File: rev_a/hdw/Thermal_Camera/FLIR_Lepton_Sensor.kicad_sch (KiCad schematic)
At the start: 0 parts

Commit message: added lepton sensor, made some other schematic progress
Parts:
- added C1501 (x3): 0.1uF, Capacitors_SMD:C_0603, symbol Custom_Library:C_Custom
- added N?: Lepton3.5 Sensor, symbol Mechanical:Housing
- added U?: FLIR_Lepton3p5_Socket, Custom Footprints Library:MOLEX_105028-1001, symbol Custom Library:FLIR_Lepton3p5_Socket
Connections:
- new net +1.2V: C1501.1, U?.7 (VDDC)
- new net +2.8V: C1501.1, U?.19 (VDD)
- new net +3.0V: C1501.1, U?.16 (VDDIO)
- new net FLIR_CLK: U?.26 (MASTER_CLK)
- new net GND: C1501.2, C1501.2, C1501.2, U?.1 (G1), U?.10 (G10), U?.15 (G15), U?.18 (G18), U?.25 (G25), U?.27 (G27), U?.30 (G30), U?.6 (G6), U?.8 (G8), U?.9 (G9), U?.P1 (SHEILD), U?.P10 (G42), U?.P11 (G43), U?.P12 (G44), U?.P13 (G45), U?.P14 (G46), U?.P15 (G47), U?.P16 (G48), U?.P17 (G49), U?.P18 (G50), U?.P19 (G51), U?.P2 (G34), U?.P20 (G52), U?.P21 (G53), U?.P22 (G54), U?.P23 (G55), U?.P24 (G56), U?.P25 (G57), U?.P26 (G58), U?.P27 (G59), U?.P28 (G60), U?.P29 (G61), U?.P3 (G35), U?.P30 (G62), U?.P31 (G63), U?.P32 (G64), U?.P33 (G65), U?.P34 (G66), U?.P35 (G67), U?.P36 (G68), U?.P4 (G36), U?.P5 (G37), U?.P6 (G38), U?.P7 (G39), U?.P8 (G40), U?.P9 (G41)
- no-connect marks 0 -> 7
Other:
- note added: "CAUTION: +3.0V I/O"
- note added: "Power Supply Considerations: VDDC: 1.20V (1.14V min, 1.26V max), 50mVpp max ripple, 110mA max draw VDD: 2.80V (2.72V min, 2.88V max), 30mVpp max ripple, 16mA max draw VDDIO: 2.8V min, 3.1V max, 50mVpp max ripple, 310mA max draw"
- note added: "See FLIR document #110-0144-04 for I2C register map"

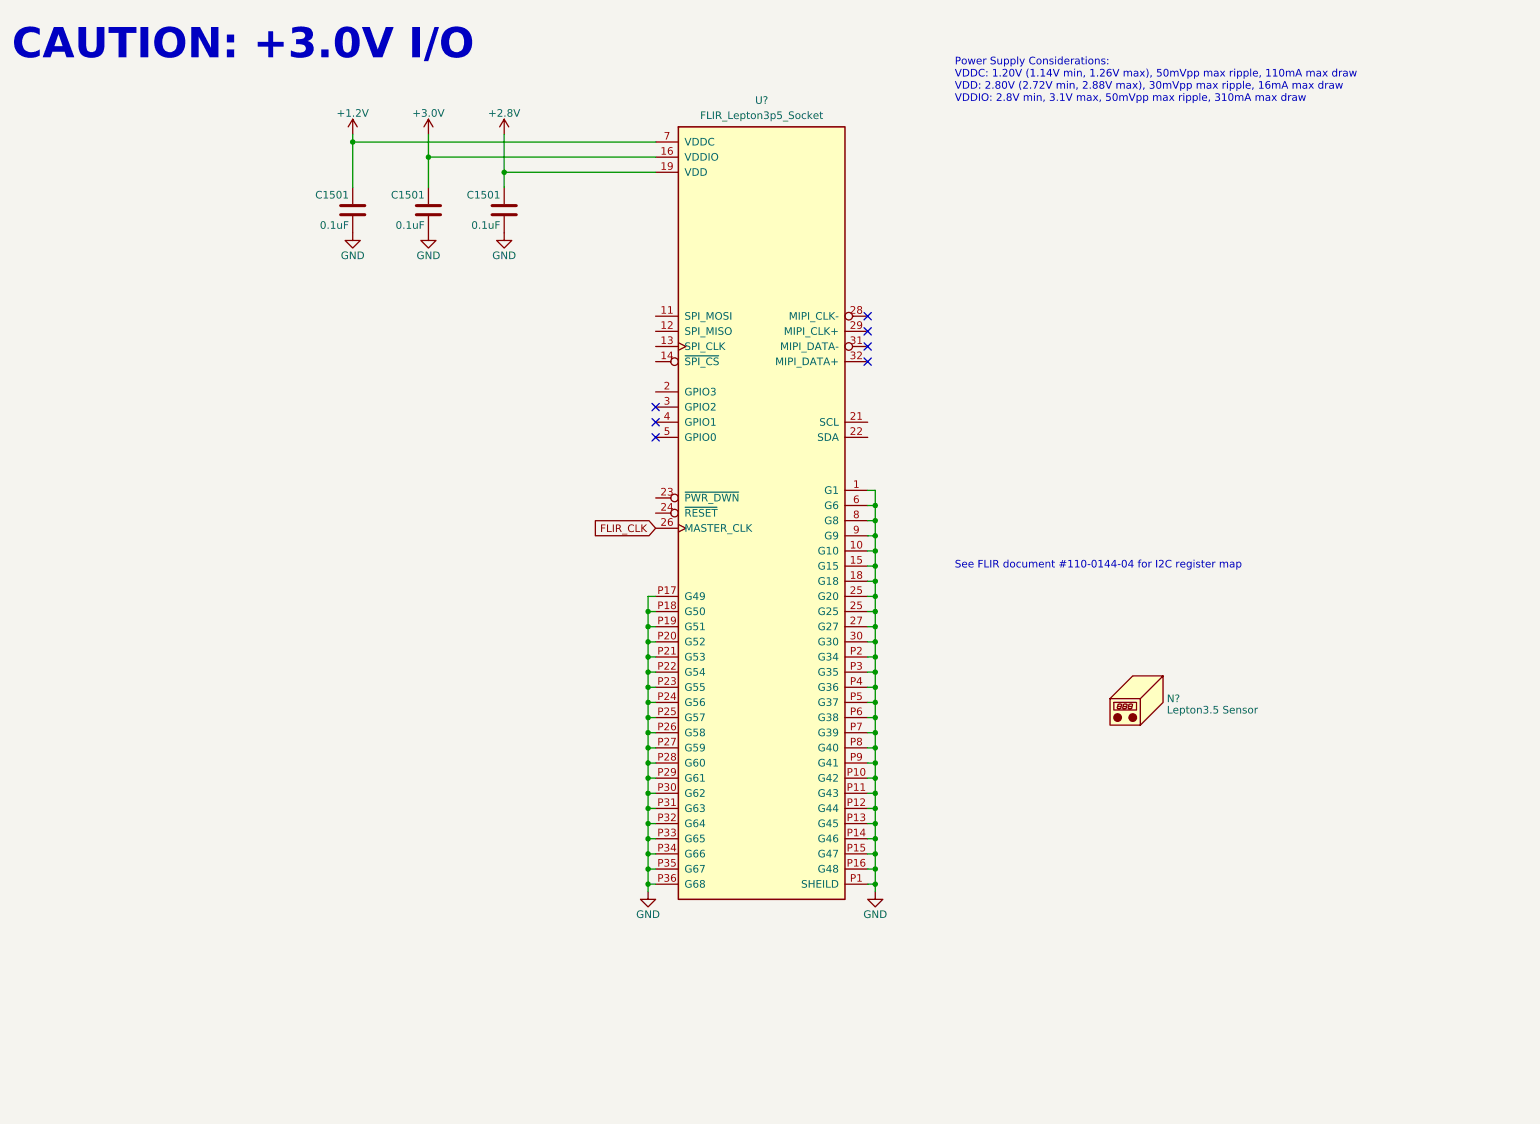
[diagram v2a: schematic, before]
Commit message: added FLIR leptson IO level shifters
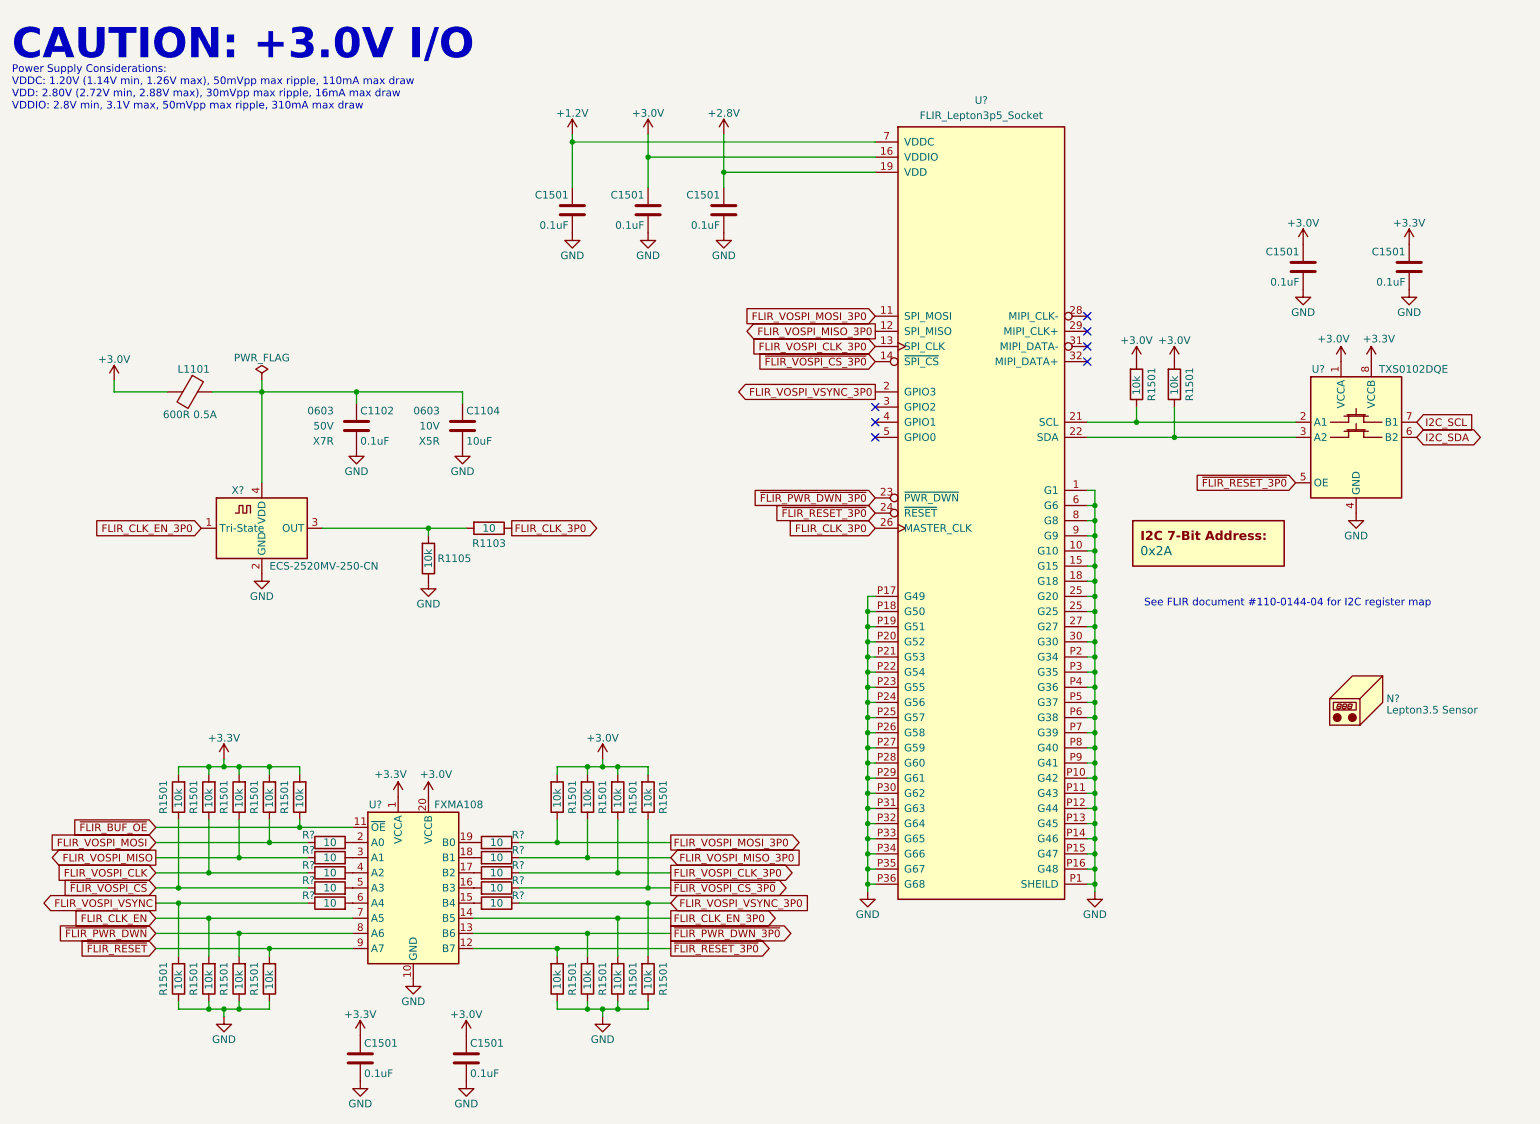
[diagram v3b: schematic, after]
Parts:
- added C1102, C1501 (x4): 0.1uF, Capacitors_SMD:C_0603, symbol Custom_Library:C_Custom
- added C1104: 10uF, Capacitors_SMD:C_0603, symbol Custom_Library:C_Custom
- added DOC?: 0x2A, symbol Custom Library:I2C_Address
- added L1101: 600R 0.5A, Inductors_SMD:L_0603, symbol Device:Ferrite_Bead
- added R1103, R? (x10): 10, Resistors_SMD:R_0603, symbol Custom_Library:R_Custom
- added R1105, R1501 (x19): 10k, Resistors_SMD:R_0603, symbol Custom_Library:R_Custom
- added U?: TXS0102DQE, Package_SON:X2SON-8_1.4x1mm_P0.35mm, symbol Custom Library:TXS0102DQE
- added U?: FXMA108, Package_DFN_QFN:WQFN-20-1EP_2.5x4.5mm_P0.5mm_EP1x2.9mm, symbol Logic_LevelTranslator:FXMA108
- added X?: ECS-2520MV-250-CN, Oscillator:Oscillator_SMD_ECS_2520MV-xxx-xx-4Pin_2.5x2.0mm, symbol Oscillator:ECS-2520MV-xxx-xx
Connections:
- net +3.0V: now also C1501.1, C1501.1, L1101.2, R1501.1, R1501.1, R1501.1, R1501.1, R1501.1, R1501.1, U?.1 (VCCA), U?.20 (VCCB)
- net GND: now also C1102.2, C1104.2, C1501.2, C1501.2, C1501.2, C1501.2, R1105.2, R1501.2, R1501.2, R1501.2, R1501.2, R1501.2, R1501.2, R1501.2, R1501.2, U?.10 (GND), U?.4 (GND), X?.2 (GND)
- net FLIR_VOSPI_MOSI_3P0: now reaches U?.11 (SPI_MOSI)
- net FLIR_VOSPI_MOSI_3P0: now also R1501.2, R?.2
- net FLIR_VOSPI_MISO_3P0: now reaches U?.12 (SPI_MISO)
- net FLIR_VOSPI_MISO_3P0: now also R1501.2, R?.2
- net FLIR_VOSPI_CLK_3P0: now reaches U?.13 (SPI_CLK)
- net FLIR_VOSPI_CLK_3P0: now also R1501.2, R?.2
- net ~{FLIR_VOSPI_CS_3P0}: now reaches U?.14 (~{SPI_CS})
- net ~{FLIR_VOSPI_CS_3P0}: now also R1501.2, R?.2
- net FLIR_VOSPI_VSYNC_3P0: now reaches U?.2 (GPIO3)
- net FLIR_VOSPI_VSYNC_3P0: now also R1501.1, R?.2
- net at U?.21 (SCL): now also R1501.2, U?.2 (A1)
- net at U?.22 (SDA): now also R1501.2, U?.3 (A2)
- net ~{FLIR_PWR_DWN_3P0}: now reaches U?.23 (~{PWR_DWN})
- net ~{FLIR_PWR_DWN_3P0}: now also R1501.1, U?.13 (B6)
- net ~{FLIR_RESET_3P0}: now reaches U?.24 (~{RESET})
- net ~{FLIR_RESET_3P0}: now also R1501.1, U?.12 (B7), U?.5 (OE)
- net FLIR_CLK renamed FLIR_CLK_3P0
- net FLIR_CLK_3P0: now also R1103.2
- new net: R1103.1, R1105.1, X?.3 (OUT)
- new net: R?.1, U?.6 (A4)
- new net: C1102.1, C1104.1, L1101.1, X?.4 (VDD)
- new net: R?.1, U?.17 (B2)
- new net: R?.1, U?.15 (B4)
- new net: R?.1, U?.4 (A2)
- new net: R?.1, U?.18 (B1)
- new net: R?.1, U?.5 (A3)
- new net: R?.1, U?.16 (B3)
- new net: R?.1, U?.19 (B0)
- new net: R?.1, U?.2 (A0)
- new net: R?.1, U?.3 (A1)
- new net +3.3V: C1501.1, C1501.1, R1501.1, R1501.1, R1501.1, R1501.1, R1501.1, U?.1 (VCCA), U?.8 (VCCB)
- new net FLIR_CLK_EN: R1501.1, U?.7 (A5)
- new net FLIR_CLK_EN_3P0: R1501.1, U?.14 (B5), X?.1 (Tri-State)
- new net FLIR_VOSPI_CLK: R1501.2, R?.2
- new net FLIR_VOSPI_MISO: R1501.2, R?.2
- new net FLIR_VOSPI_MOSI: R1501.2, R?.2
- new net FLIR_VOSPI_VSYNC: R1501.1, R?.2
- new net I2C_SCL: U?.7 (B1)
- new net I2C_SDA: U?.6 (B2)
- new net ~{FLIR_BUF_OE}: R1501.2, U?.11 (~{OE})
- new net ~{FLIR_PWR_DWN}: R1501.1, U?.8 (A6)
- new net ~{FLIR_RESET}: R1501.1, U?.9 (A7)
- new net ~{FLIR_VOSPI_CS}: R1501.2, R?.2
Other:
- moved on the sheet: C1501, N?, U?

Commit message: changed a lot of circuits from +3.3V to +3.0V VDD
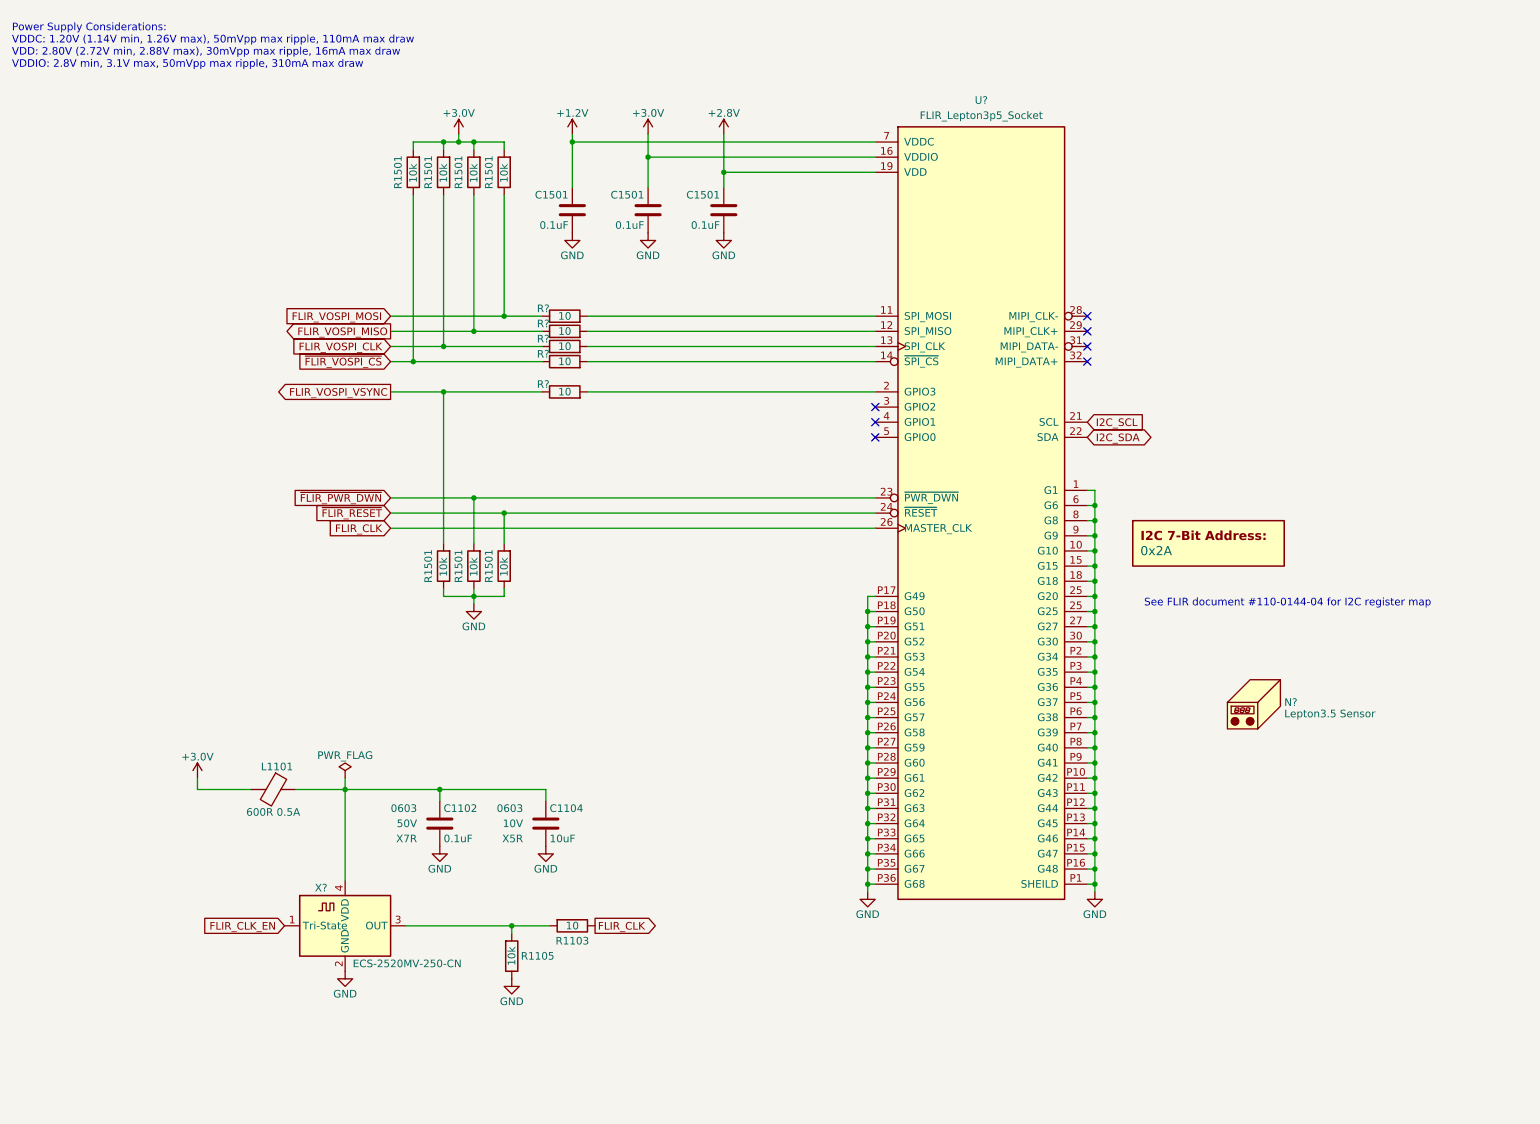
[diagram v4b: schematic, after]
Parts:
- removed C1501 (x4): 0.1uF, Capacitors_SMD:C_0603, symbol Custom_Library:C_Custom
- removed R1501 (x13): 10k, Resistors_SMD:R_0603, symbol Custom_Library:R_Custom
- removed R? (x5): 10, Resistors_SMD:R_0603, symbol Custom_Library:R_Custom
- removed U?: TXS0102DQE, Package_SON:X2SON-8_1.4x1mm_P0.35mm, symbol Custom Library:TXS0102DQE
- removed U?: FXMA108, Package_DFN_QFN:WQFN-20-1EP_2.5x4.5mm_P0.5mm_EP1x2.9mm, symbol Logic_LevelTranslator:FXMA108
- added R1501: 10k, Resistors_SMD:R_0603, symbol Custom_Library:R_Custom
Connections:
- net +3.3V is gone; now on net +3.0V: R1501.1, R1501.1, R1501.1, R1501.1
- net FLIR_CLK_EN_3P0 is gone; now on net FLIR_CLK_EN: X?.1 (Tri-State)
- net FLIR_VOSPI_CLK_3P0 is gone; now on an unnamed net: U?.13 (SPI_CLK)
- net FLIR_VOSPI_MISO_3P0 is gone; now on an unnamed net: U?.12 (SPI_MISO)
- net FLIR_VOSPI_MOSI_3P0 is gone; now on an unnamed net: U?.11 (SPI_MOSI)
- net FLIR_VOSPI_VSYNC_3P0 is gone; now on an unnamed net: U?.2 (GPIO3)
- net ~{FLIR_PWR_DWN_3P0} is gone; now on net ~{FLIR_PWR_DWN}: U?.23 (~{PWR_DWN})
- net ~{FLIR_RESET_3P0} is gone; now on net ~{FLIR_RESET}: U?.24 (~{RESET})
- net ~{FLIR_VOSPI_CS_3P0} is gone; now on an unnamed net: U?.14 (~{SPI_CS})
- net FLIR_VOSPI_VSYNC: now also R1501.1
- net GND: now also R1501.2
- net I2C_SCL: now also U?.21 (SCL)
- net I2C_SDA: now also U?.22 (SDA)
- net FLIR_CLK_3P0 renamed FLIR_CLK
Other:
- note removed: "CAUTION: +3.0V I/O"
- moved on the sheet: C1102, C1104, L1101, N?, R1103, R1105, R1501, R?, X?
